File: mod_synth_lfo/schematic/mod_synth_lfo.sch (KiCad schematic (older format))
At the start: 75 parts, among them J1 AudioJack2, J2 Conn_02x08_Odd_Even, J3 AudioJack2, J4 AudioJack2, J5 AudioJack2, J6 AudioJack2, J7 AudioJack2, J8 AudioJack2, Q1 BC550, Q2 BC550, Q3 BC550, Q4 BC550, Q5 BC550, U1 TL072, U2 TL072, U3 TL072, U4 TL074

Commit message: Add footprints and values
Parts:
- C1, C2: footprint (none) -> Capacitor_THT:CP_Radial_D5.0mm_P2.00mm
- C10, C11, C3, C4, C5, C6, C8, C9: footprint (none) -> Capacitor_THT:C_Disc_D9.0mm_W2.5mm_P5.00mm
- C7: value C -> 100nf; footprint (none) -> Capacitor_THT:C_Disc_D9.0mm_W2.5mm_P5.00mm
- D1: footprint (none) -> LED_THT:LED_D5.0mm
- J1: value AudioJack2 -> CV; footprint (none) -> Connector_Audio:Jack_3.5mm_QingPu_WQP-PJ398SM_Vertical_CircularHoles
- J2: footprint (none) -> Connector_IDC:IDC-Header_2x08_P2.54mm_Vertical
- J3: value AudioJack2 -> SIN; footprint (none) -> Connector_Audio:Jack_3.5mm_QingPu_WQP-PJ398SM_Vertical_CircularHoles
- J4: footprint (none) -> Connector_Audio:Jack_3.5mm_QingPu_WQP-PJ398SM_Vertical_CircularHoles
- J5: value AudioJack2 -> TRI; footprint (none) -> Connector_Audio:Jack_3.5mm_QingPu_WQP-PJ398SM_Vertical_CircularHoles
- J6: value AudioJack2 -> SQR; footprint (none) -> Connector_Audio:Jack_3.5mm_QingPu_WQP-PJ398SM_Vertical_CircularHoles
- J7: value AudioJack2 -> RAMP UP; footprint (none) -> Connector_Audio:Jack_3.5mm_QingPu_WQP-PJ398SM_Vertical_CircularHoles
- J8: value AudioJack2 -> RAMP DOWN; footprint (none) -> Connector_Audio:Jack_3.5mm_QingPu_WQP-PJ398SM_Vertical_CircularHoles
- R1, R19, R2, R20, R21, R23, R25, R3, R30, R4, R5, R6: value R -> 100k
- R10, R14, R17, R18, R29, R33, R34, R35, R38, R39: value R -> 10k
- R11, R13, R7, R8, R9: value R -> 47k
- R12, R22: value R -> 470
- R15: value R -> 220
- R16: value R -> 68k
- R24, R26: value R -> 33k
- R27: value R -> 50k
- R28: value R -> 20k
- R31: value RTRIM -> 20k
- R32, R36, R37, R40, R41, R42: value R -> 1k
- RV1: value R_POT -> SPEED
- RV2: value R_POT -> CV AMOUNT
- RV3: value R_POT -> 100k
- RV4: value R_POT_TRIM -> 50k; footprint (none) -> Potentiometer_THT:Potentiometer_Runtron_RM-065_Vertical
- U1, U2, U3: footprint (none) -> Package_DIP:DIP-8_W7.62mm_Socket_LongPads
- U4: footprint (none) -> Package_DIP:DIP-14_W7.62mm_Socket_LongPads

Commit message: Attempt to layout PCB
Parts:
- removed R31: 20k, symbol Device:RTRIM
- added RV5: 20k, Potentiometer_THT:Potentiometer_Runtron_RM-065_Vertical, symbol Device:R_POT
- C1, C2: value CP -> 10uf
- C10, C11, C3, C4, C5, C6, C8, C9: value C -> 100nf
- J4: value AudioJack2 -> COS
- RV3: footprint Potentiometer_THT:Potentiometer_Alpha_RD901F-40-00D_Single_Vertical_CircularHoles -> Potentiometer_THT:Potentiometer_Runtron_RM-065_Vertical
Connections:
- net GND: now also RV5.2
- net at R27.1, U4.5 (+): now also RV5.1
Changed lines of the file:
@@
 P 9500 1925
 F 0 "J4" H 9320 2000 50  0000 R CNN
-F 1 "AudioJack2" H 9320 1909 50  0000 R CNN
+F 1 "COS" H 9320 1909 50  0000 R CNN
 F 2 "Connector_Audio:Jack_3.5mm_QingPu_WQP-PJ398SM_Vertical_CircularHoles" H 9500 1925 50  0001 C CNN
 F 3 "~" H 9500 1925 50  0001 C CNN
@@
 F 0 "RV3" V 5160 1650 50  0000 C CNN
 F 1 "100k" V 5069 1650 50  0000 C CNN
-F 2 "Potentiometer_THT:Potentiometer_Alpha_RD901F-40-00D_Single_Vertical_CircularHoles" H 5275 1650 50  0001 C CNN
+F 2 "Potentiometer_THT:Potentiometer_Runtron_RM-065_Vertical" H 5275 1650 50  0001 C CNN
 F 3 "~" H 5275 1650 50  0001 C CNN
 	1    5275 1650
@@
 L power:GND #PWR0118
 U 1 1 5D62F449
-P 8475 5550
-F 0 "#PWR0118" H 8475 5300 50  0001 C CNN
-F 1 "GND" H 8480 5377 50  0000 C CNN
-F 2 "" H 8475 5550 50  0001 C CNN
-F 3 "" H 8475 5550 50  0001 C CNN
-	1    8475 5550
-	1    0    0    -1
-$EndComp
-$Comp
-L Device:RTRIM R31
-U 1 1 5D62F9A2
-P 8225 5450
-F 0 "R31" V 7985 5450 50  0000 C CNN
-F 1 "20k" V 8076 5450 50  0000 C CNN
-F 2 "" V 8155 5450 50  0001 C CNN
-F 3 "~" H 8225 5450 50  0001 C CNN
-	1    8225 5450
-	0    1    1    0
+P 8225 5700
+F 0 "#PWR0118" H 8225 5450 50  0001 C CNN
+F 1 "GND" H 8230 5527 50  0000 C CNN
+F 2 "" H 8225 5700 50  0001 C CNN
+F 3 "" H 8225 5700 50  0001 C CNN
+	1    8225 5700
+	1    0    0    -1
 $EndComp
 Wire Wire Line
@@
 	7950 5450 7950 5625
 Wire Wire Line
-	8375 5450 8475 5450
-Wire Wire Line
-	8475 5450 8475 5550
+	8225 5600 8225 5700
 Wire Wire Line
 	9025 6300 8925 6300
@@
 P 3800 6150
 F 0 "C3" H 3915 6196 50  0000 L CNN
-F 1 "C" H 3915 6105 50  0000 L CNN
+F 1 "100nf" H 3915 6105 50  0000 L CNN
 F 2 "Capacitor_THT:C_Disc_D9.0mm_W2.5mm_P5.00mm" H 3838 6000 50  0001 C CNN
 F 3 "~" H 3800 6150 50  0001 C CNN
@@
 P 4300 6150
 F 0 "C5" H 4415 6196 50  0000 L CNN
-F 1 "C" H 4415 6105 50  0000 L CNN
+F 1 "100nf" H 4415 6105 50  0000 L CNN
 F 2 "Capacitor_THT:C_Disc_D9.0mm_W2.5mm_P5.00mm" H 4338 6000 50  0001 C CNN
 F 3 "~" H 4300 6150 50  0001 C CNN
@@
 P 4850 6150
 F 0 "C8" H 4965 6196 50  0000 L CNN
-F 1 "C" H 4965 6105 50  0000 L CNN
+F 1 "100nf" H 4965 6105 50  0000 L CNN
 F 2 "Capacitor_THT:C_Disc_D9.0mm_W2.5mm_P5.00mm" H 4888 6000 50  0001 C CNN
 F 3 "~" H 4850 6150 50  0001 C CNN
@@
 P 5325 6150
 F 0 "C10" H 5440 6196 50  0000 L CNN
-F 1 "C" H 5440 6105 50  0000 L CNN
+F 1 "100nf" H 5440 6105 50  0000 L CNN
 F 2 "Capacitor_THT:C_Disc_D9.0mm_W2.5mm_P5.00mm" H 5363 6000 50  0001 C CNN
 F 3 "~" H 5325 6150 50  0001 C CNN
@@
 P 5325 7375
 F 0 "C11" H 5440 7421 50  0000 L CNN
-F 1 "C" H 5440 7330 50  0000 L CNN
+F 1 "100nf" H 5440 7330 50  0000 L CNN
 F 2 "Capacitor_THT:C_Disc_D9.0mm_W2.5mm_P5.00mm" H 5363 7225 50  0001 C CNN
 F 3 "~" H 5325 7375 50  0001 C CNN
@@
 P 4850 7375
 F 0 "C9" H 4965 7421 50  0000 L CNN
-F 1 "C" H 4965 7330 50  0000 L CNN
+F 1 "100nf" H 4965 7330 50  0000 L CNN
 F 2 "Capacitor_THT:C_Disc_D9.0mm_W2.5mm_P5.00mm" H 4888 7225 50  0001 C CNN
 F 3 "~" H 4850 7375 50  0001 C CNN
@@
 P 4300 7375
 F 0 "C6" H 4415 7421 50  0000 L CNN
-F 1 "C" H 4415 7330 50  0000 L CNN
+F 1 "100nf" H 4415 7330 50  0000 L CNN
 F 2 "Capacitor_THT:C_Disc_D9.0mm_W2.5mm_P5.00mm" H 4338 7225 50  0001 C CNN
 F 3 "~" H 4300 7375 50  0001 C CNN
@@
 P 3800 7375
 F 0 "C4" H 3915 7421 50  0000 L CNN
-F 1 "C" H 3915 7330 50  0000 L CNN
+F 1 "100nf" H 3915 7330 50  0000 L CNN
 F 2 "Capacitor_THT:C_Disc_D9.0mm_W2.5mm_P5.00mm" H 3838 7225 50  0001 C CNN
 F 3 "~" H 3800 7375 50  0001 C CNN
@@
 P 1725 7175
 F 0 "C2" H 1843 7221 50  0000 L CNN
-F 1 "CP" H 1843 7130 50  0000 L CNN
+F 1 "10uf" H 1843 7130 50  0000 L CNN
 F 2 "Capacitor_THT:CP_Radial_D5.0mm_P2.00mm" H 1763 7025 50  0001 C CNN
 F 3 "~" H 1725 7175 50  0001 C CNN
@@
 P 1725 6450
 F 0 "C1" H 1843 6496 50  0000 L CNN
-F 1 "CP" H 1843 6405 50  0000 L CNN
+F 1 "10uf" H 1843 6405 50  0000 L CNN
 F 2 "Capacitor_THT:CP_Radial_D5.0mm_P2.00mm" H 1763 6300 50  0001 C CNN
 F 3 "~" H 1725 6450 50  0001 C CNN
@@
 Wire Notes Line
 	10925 4350 10925 6525
+$Comp
+L Device:R_POT RV5
+U 1 1 5D57C0B1
+P 8225 5450
+F 0 "RV5" V 8110 5450 50  0000 C CNN
+F 1 "20k" V 8019 5450 50  0000 C CNN
+F 2 "Potentiometer_THT:Potentiometer_Runtron_RM-065_Vertical" H 8225 5450 50  0001 C CNN
+F 3 "~" H 8225 5450 50  0001 C CNN
+	1    8225 5450
+	0    -1   1    0
+$EndComp
 $EndSCHEMATC

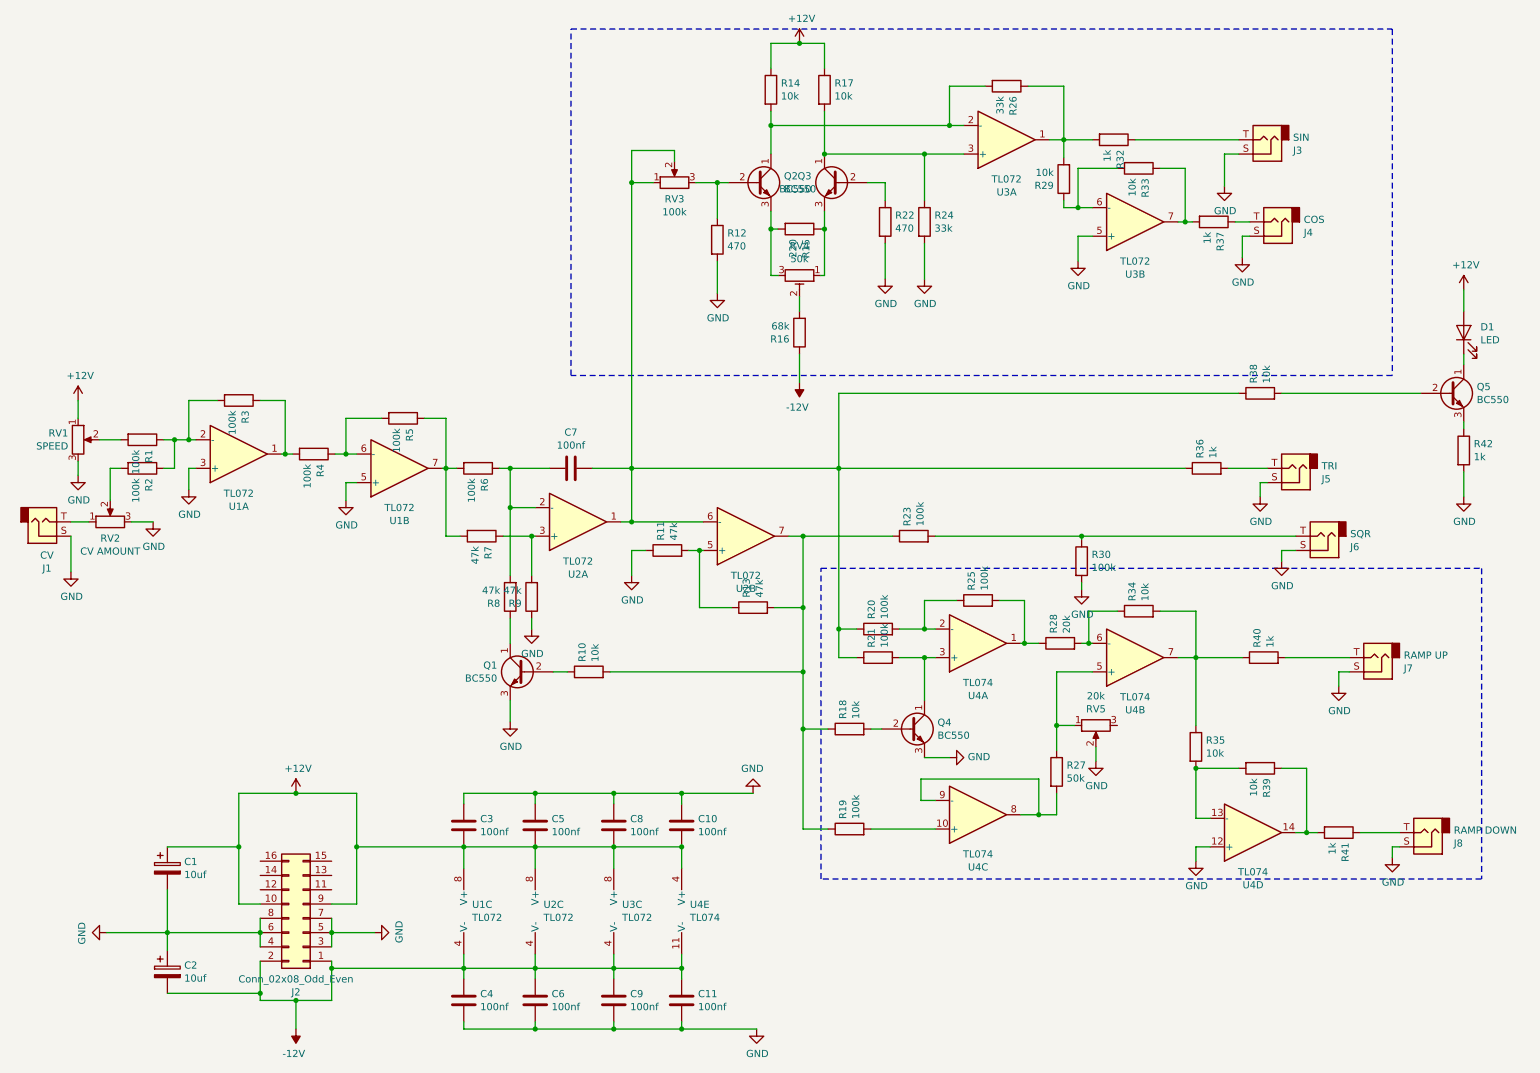
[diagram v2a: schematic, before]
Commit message: Remove ramp and sin outputs
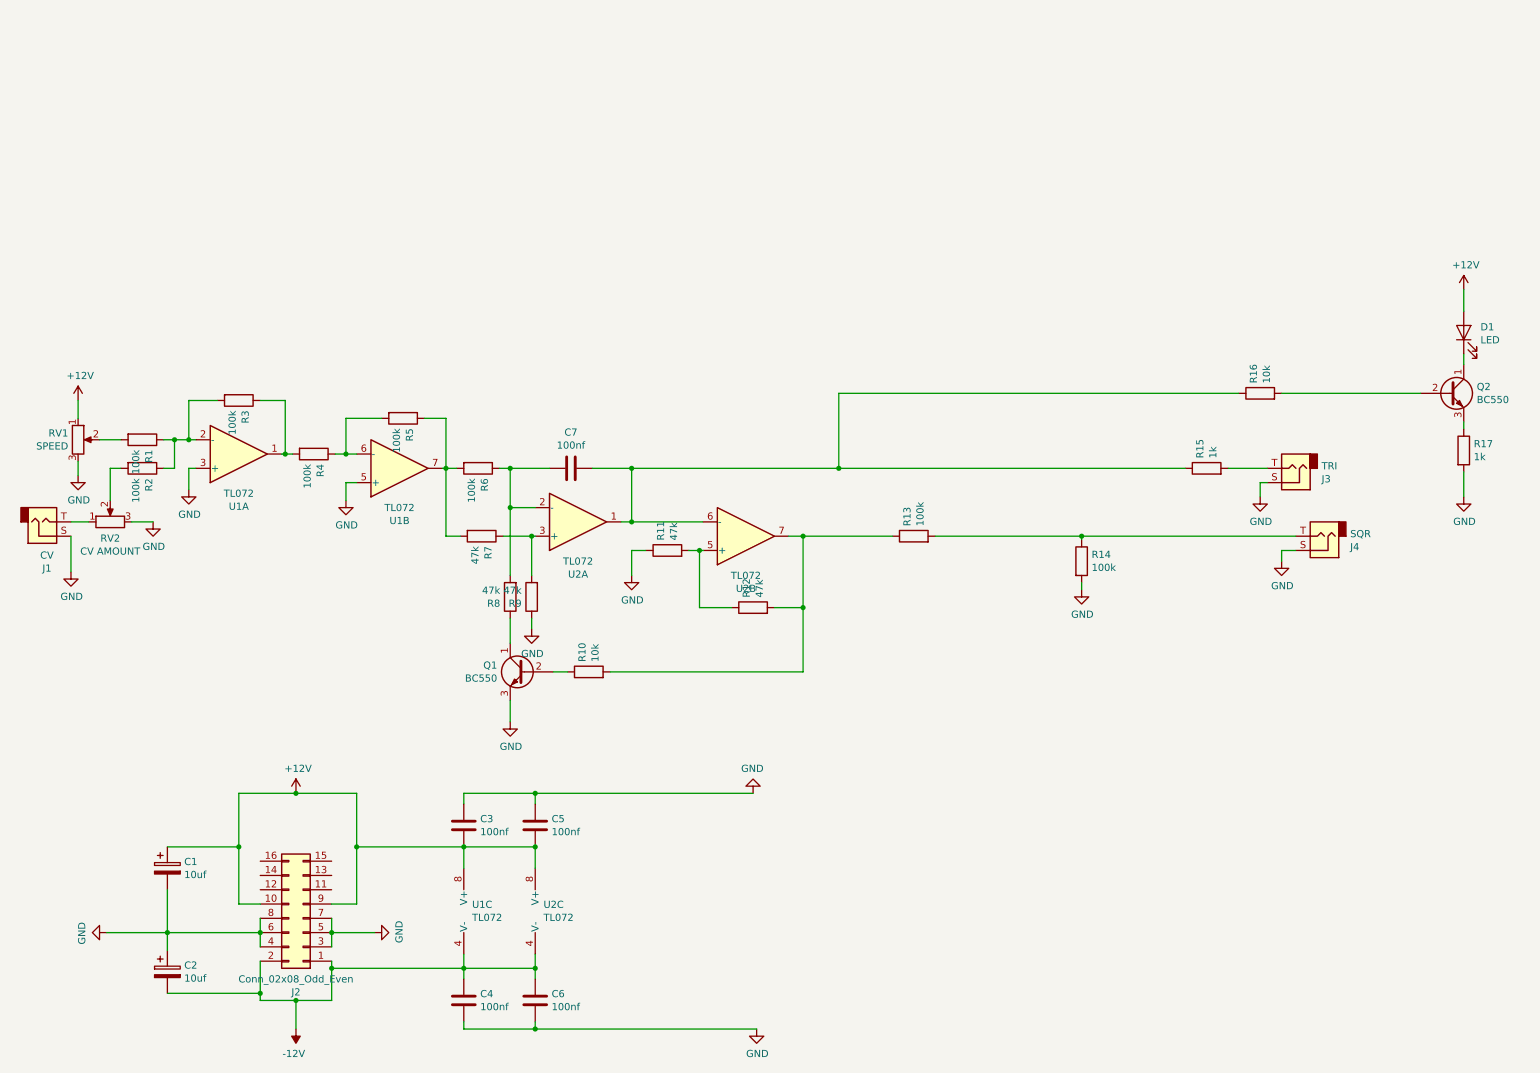
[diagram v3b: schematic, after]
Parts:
- removed C10, C11, C8, C9: 100nf, Capacitor_THT:C_Disc_D9.0mm_W2.5mm_P5.00mm, symbol Device:C
- removed J3: SIN, Connector_Audio:Jack_3.5mm_QingPu_WQP-PJ398SM_Vertical_CircularHoles, symbol Connector:AudioJack2
- removed J4: COS, Connector_Audio:Jack_3.5mm_QingPu_WQP-PJ398SM_Vertical_CircularHoles, symbol Connector:AudioJack2
- removed J7: RAMP UP, Connector_Audio:Jack_3.5mm_QingPu_WQP-PJ398SM_Vertical_CircularHoles, symbol Connector:AudioJack2
- removed J8: RAMP DOWN, Connector_Audio:Jack_3.5mm_QingPu_WQP-PJ398SM_Vertical_CircularHoles, symbol Connector:AudioJack2
- removed Q2, Q3, Q4: BC550, Package_TO_SOT_THT:TO-92_Inline, symbol Transistor_BJT:BC550
- removed R12, R22: 470, Resistor_THT:R_Axial_DIN0207_L6.3mm_D2.5mm_P10.16mm_Horizontal, symbol Device:R
- removed R14, R17, R18, R29, R33, R34, R35, R39: 10k, Resistor_THT:R_Axial_DIN0207_L6.3mm_D2.5mm_P10.16mm_Horizontal, symbol Device:R
- removed R15: 220, Resistor_THT:R_Axial_DIN0207_L6.3mm_D2.5mm_P10.16mm_Horizontal, symbol Device:R
- removed R16: 68k, Resistor_THT:R_Axial_DIN0207_L6.3mm_D2.5mm_P10.16mm_Horizontal, symbol Device:R
- removed R19, R20, R21, R25: 100k, Resistor_THT:R_Axial_DIN0207_L6.3mm_D2.5mm_P10.16mm_Horizontal, symbol Device:R
- removed R24, R26: 33k, Resistor_THT:R_Axial_DIN0207_L6.3mm_D2.5mm_P10.16mm_Horizontal, symbol Device:R
- removed R27: 50k, Resistor_THT:R_Axial_DIN0207_L6.3mm_D2.5mm_P10.16mm_Horizontal, symbol Device:R
- removed R28: 20k, Resistor_THT:R_Axial_DIN0207_L6.3mm_D2.5mm_P10.16mm_Horizontal, symbol Device:R
- removed R32, R37, R40, R41: 1k, Resistor_THT:R_Axial_DIN0207_L6.3mm_D2.5mm_P10.16mm_Horizontal, symbol Device:R
- removed RV3: 100k, Potentiometer_THT:Potentiometer_Runtron_RM-065_Vertical, symbol Device:R_POT
- removed RV4: 50k, Potentiometer_THT:Potentiometer_Runtron_RM-065_Vertical, symbol Device:R_POT_TRIM
- removed RV5: 20k, Potentiometer_THT:Potentiometer_Runtron_RM-065_Vertical, symbol Device:R_POT
- removed U3: TL072, Package_DIP:DIP-8_W7.62mm_Socket_LongPads, symbol Amplifier_Operational:TL072
- removed U4: TL074, Package_DIP:DIP-14_W7.62mm_Socket_LongPads, symbol Amplifier_Operational:TL074
- renumbered J5 to J3, J6 to J4, Q5 to Q2, R13 to R12, R23 to R13, R30 to R14, R36 to R15, R38 to R16, R42 to R17

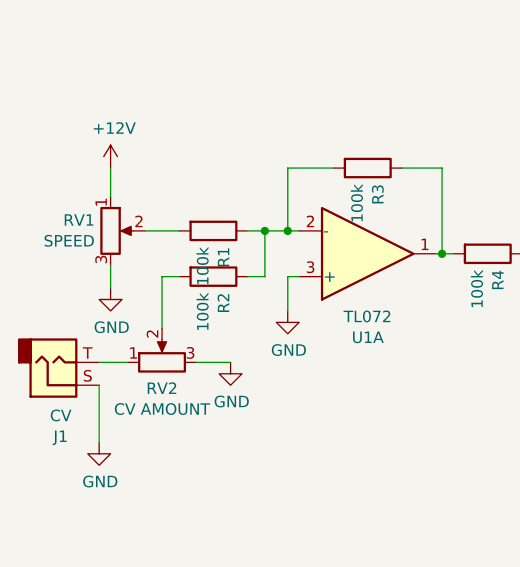
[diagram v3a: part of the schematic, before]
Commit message: Reverse pots
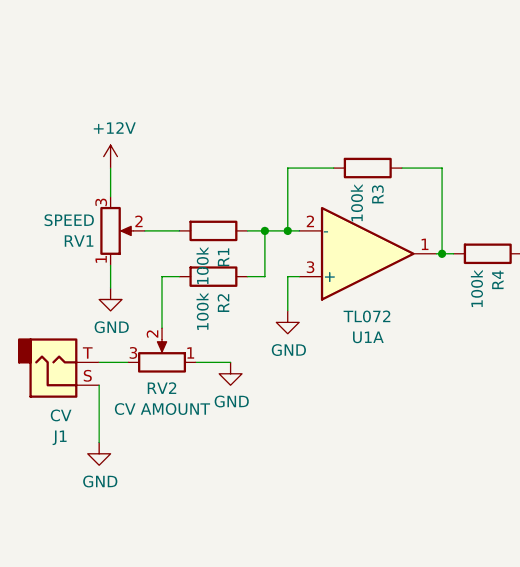
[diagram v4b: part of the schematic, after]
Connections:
- net +12V: now also RV1.3; no longer RV1.1
- net GND: now also RV1.1, RV2.1; no longer RV1.3, RV2.3
- net at J1.T: now also RV2.3; no longer RV2.1
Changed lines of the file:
@@
 F 3 "~" H 1100 3450 50  0001 C CNN
 	1    1100 3450
-	1    0    0    -1
+	1    0    0    1
 $EndComp
 $Comp
@@
 F 3 "~" H 1325 4025 50  0001 C CNN
 	1    1325 4025
-	0    -1   -1   0
+	0    1    -1   0
 $EndComp
 $Comp
